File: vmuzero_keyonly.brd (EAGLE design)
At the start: 41.4 x 65.2 mm, 10 parts

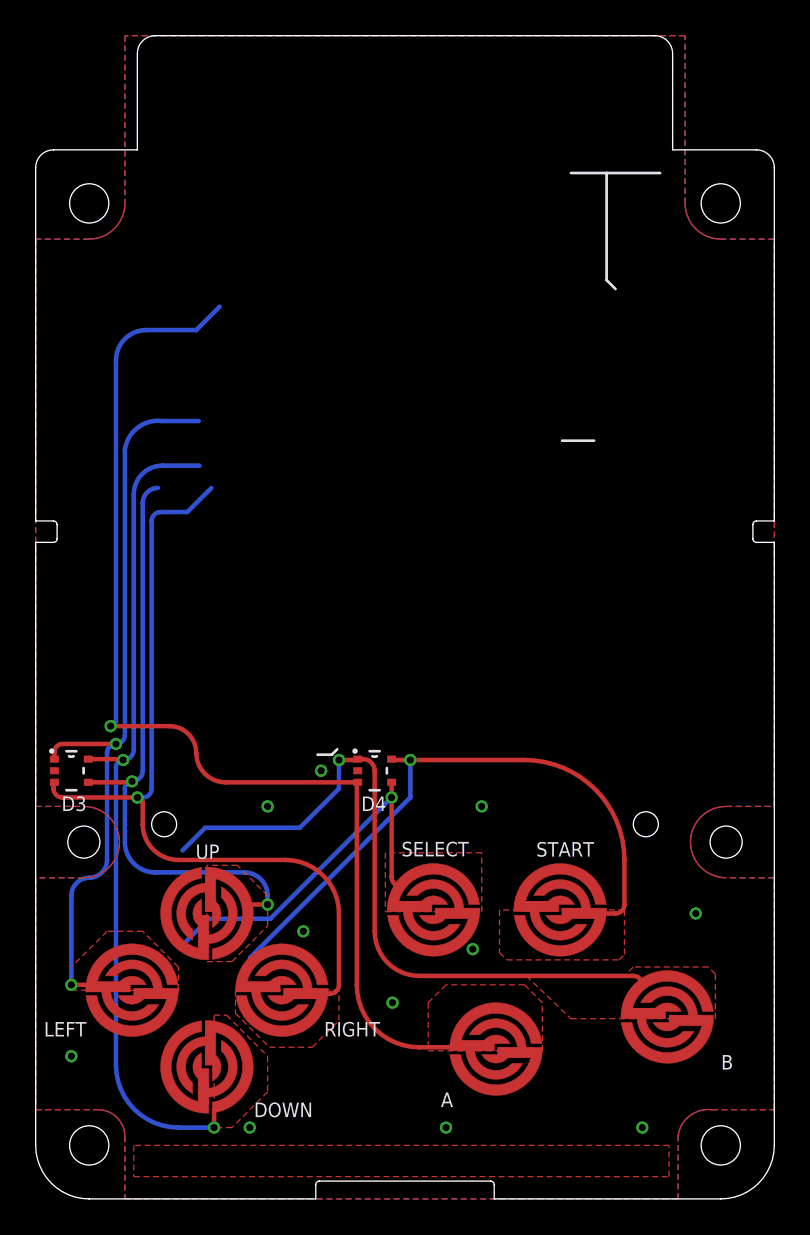
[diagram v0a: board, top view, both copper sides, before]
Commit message: Changed height to 24.5
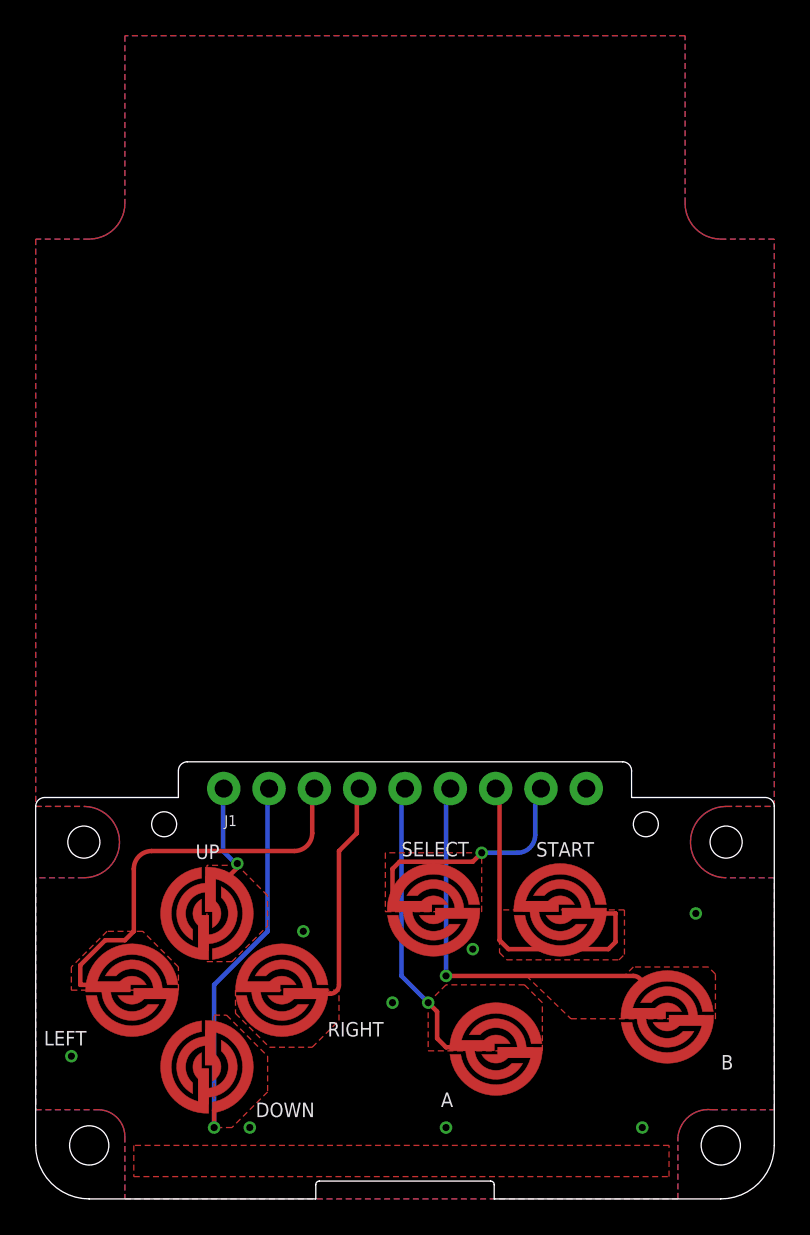
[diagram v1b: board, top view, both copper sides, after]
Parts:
- removed D3, D4: SP1001-04J, vmuzero:SC70-5
- added J1: KEY, SparkFun-Connectors:1X09_NO_SILK
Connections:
- net GND: now also J1.9; no longer D3.2, D4.2
- net KEY_A: now also J1.5; no longer D4.3
- net KEY_B: now also J1.6; no longer D4.1
- net KEY_DOWN: now also J1.2; no longer D3.5
- net KEY_LEFT: now also J1.3; no longer D3.1
- net KEY_RIGHT: now also J1.4; no longer D3.3
- net KEY_SELECT: now also J1.8; no longer D4.4
- net KEY_START: now also J1.7; no longer D4.5
- net KEY_UP: now also J1.1; no longer D3.4
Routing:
- net KEY_A: track 62.5 -> 17.5 mm
- net KEY_RIGHT: track 46.4 -> 13.8 mm, vias 1 -> 0
- net KEY_UP: track 38.0 -> 9.71 mm, vias 2 -> 1
- net KEY_DOWN: track 54.3 -> 28.9 mm, vias 2 -> 1
- net KEY_LEFT: track 42.3 -> 23.6 mm, vias 2 -> 0
- net KEY_B: track 42.4 -> 24.9 mm
- net KEY_START: track 35.4 -> 19.1 mm, vias 1 -> 0
- net KEY_SELECT: track 23.4 -> 15.0 mm
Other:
- board size 41.4 x 65.2 mm -> 41.4 x 24.5 mm
